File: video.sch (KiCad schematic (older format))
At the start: 42 parts, among them P1 VIDEO OUT, P11 I²C PORT, P2 RGBHV TEST POINTS, U1 VGA SYNC/JOY BUFFER, U2 VGA RGB BUFFER, U3 E-DDC I²C BUFFER

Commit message: Cambios menores
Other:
- note added: "Decoupling capacitors. \nPlace as close as possible to the affected IC pin."
- note added: "U1 (2 of 8)"
- note added: "U2"
- moved on the sheet: C1, C12, C13, C2, C3, C4, C5, C6, C7, R21, R22

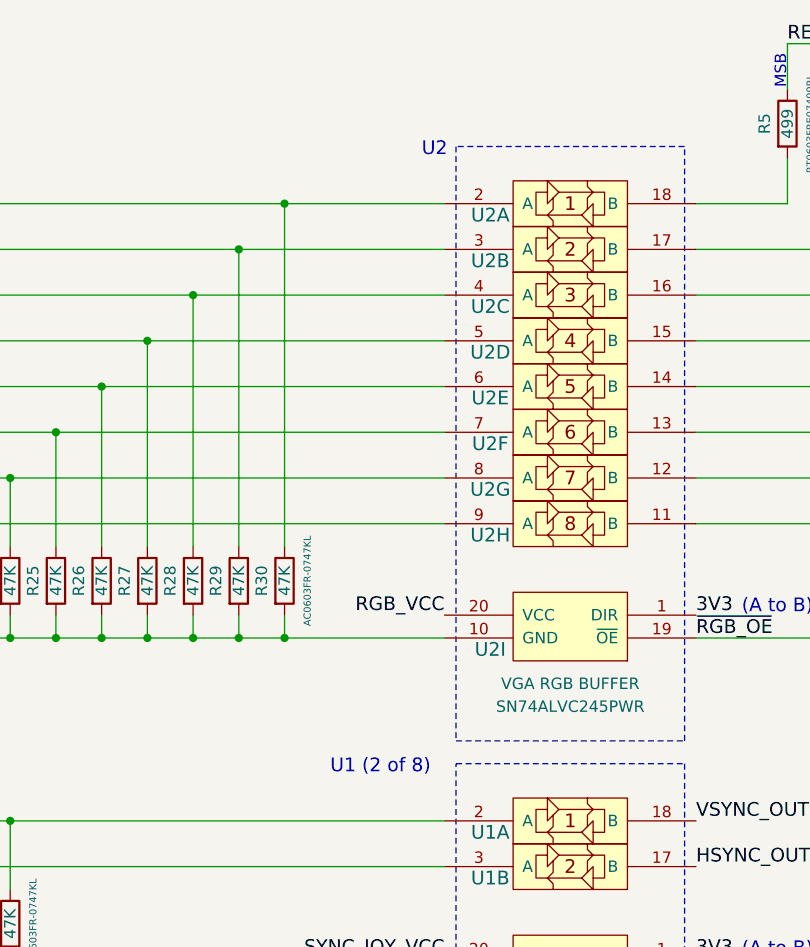
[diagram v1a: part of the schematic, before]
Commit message: Nuevo layout, mejoras y modificaciones del revisor
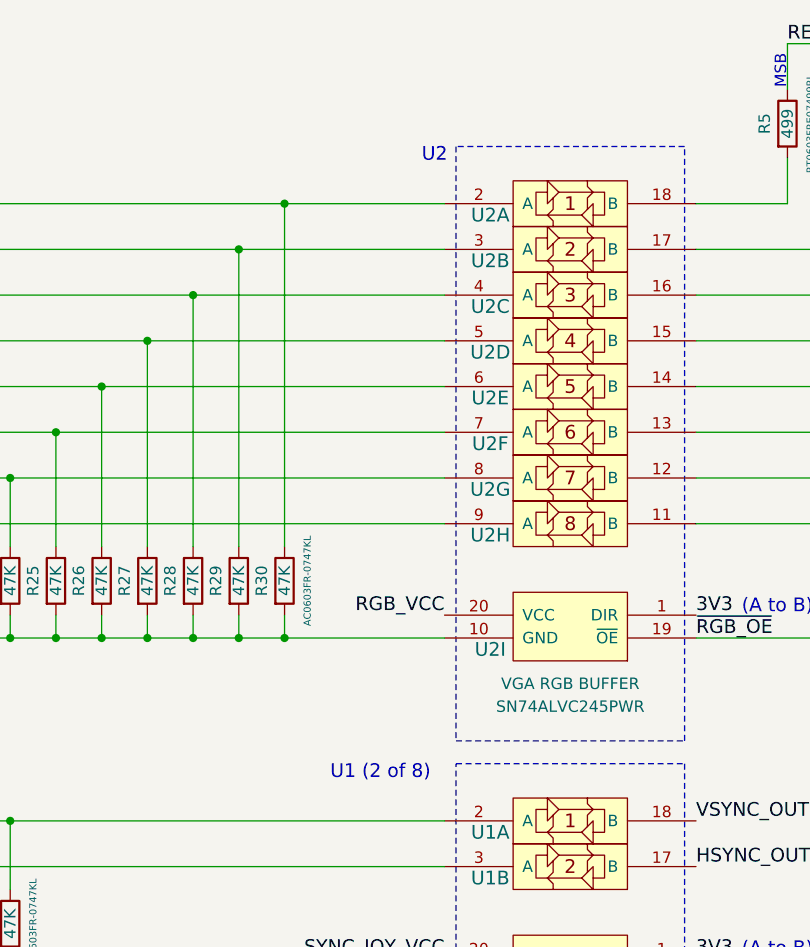
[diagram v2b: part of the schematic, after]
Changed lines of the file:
@@
 LIBS:contrib
 LIBS:valves
-LIBS:salmon
+LIBS:retro-ciaa
 LIBS:retro-ciaa-cache
 EELAYER 25 0
@@
 encoding utf-8
 Sheet 2 8
-Title "RETRO-CIAA / VIDEO"
-Date "2018-10-19"
+Title "VIDEO OUTPUT"
+Date "2018-10-20"
 Rev "1.1.1"
-Comp "Salmon Robotics"
+Comp "http://www.retro-ciaa.com"
 Comment1 "All resistors 1% & 0603\" unless otherwise noted"
 Comment2 "ERC check OK on 2018-10-19"
@@
 Text Notes 1000 7600 0    60   ~ 0
 Decoupling capacitors. \nPlace as close as possible to the affected IC pin.
-Text Notes 3400 1300 0    60   ~ 0
+Text Notes 3400 1325 0    60   ~ 0
 U2
-Text Notes 3000 4000 0    60   ~ 0
+Text Notes 3000 4025 0    60   ~ 0
 U1 (2 of 8)
 $EndSCHEMATC

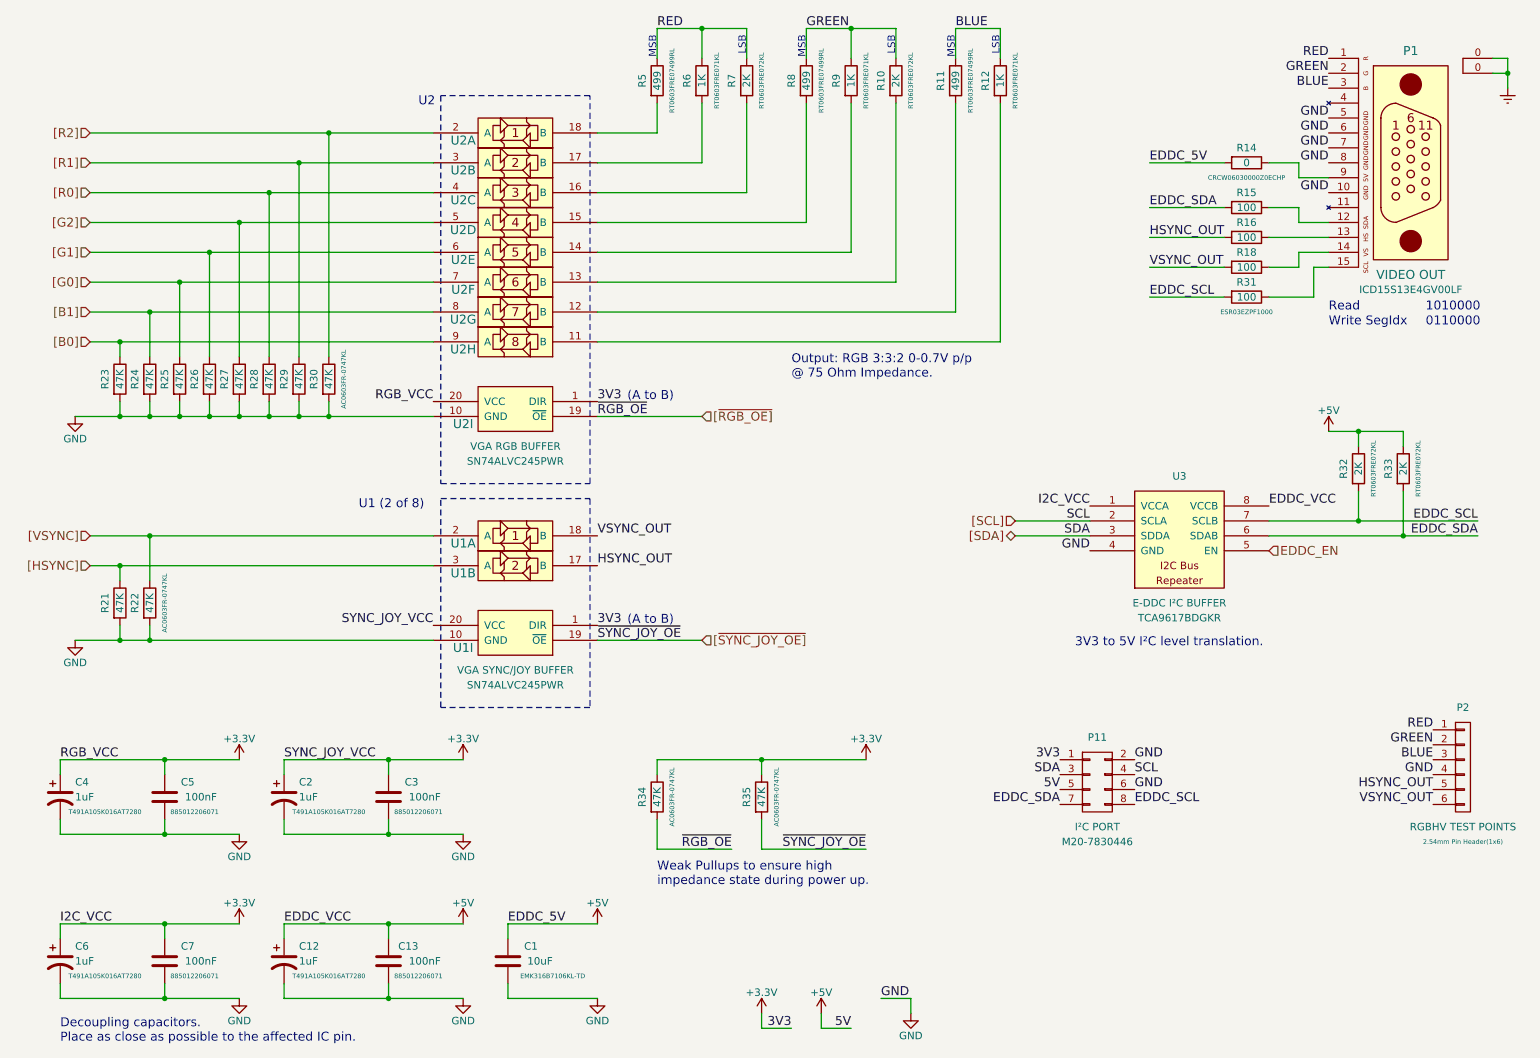
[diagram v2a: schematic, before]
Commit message: Modificacion para clarificar uso de multiparte en U1 y U2
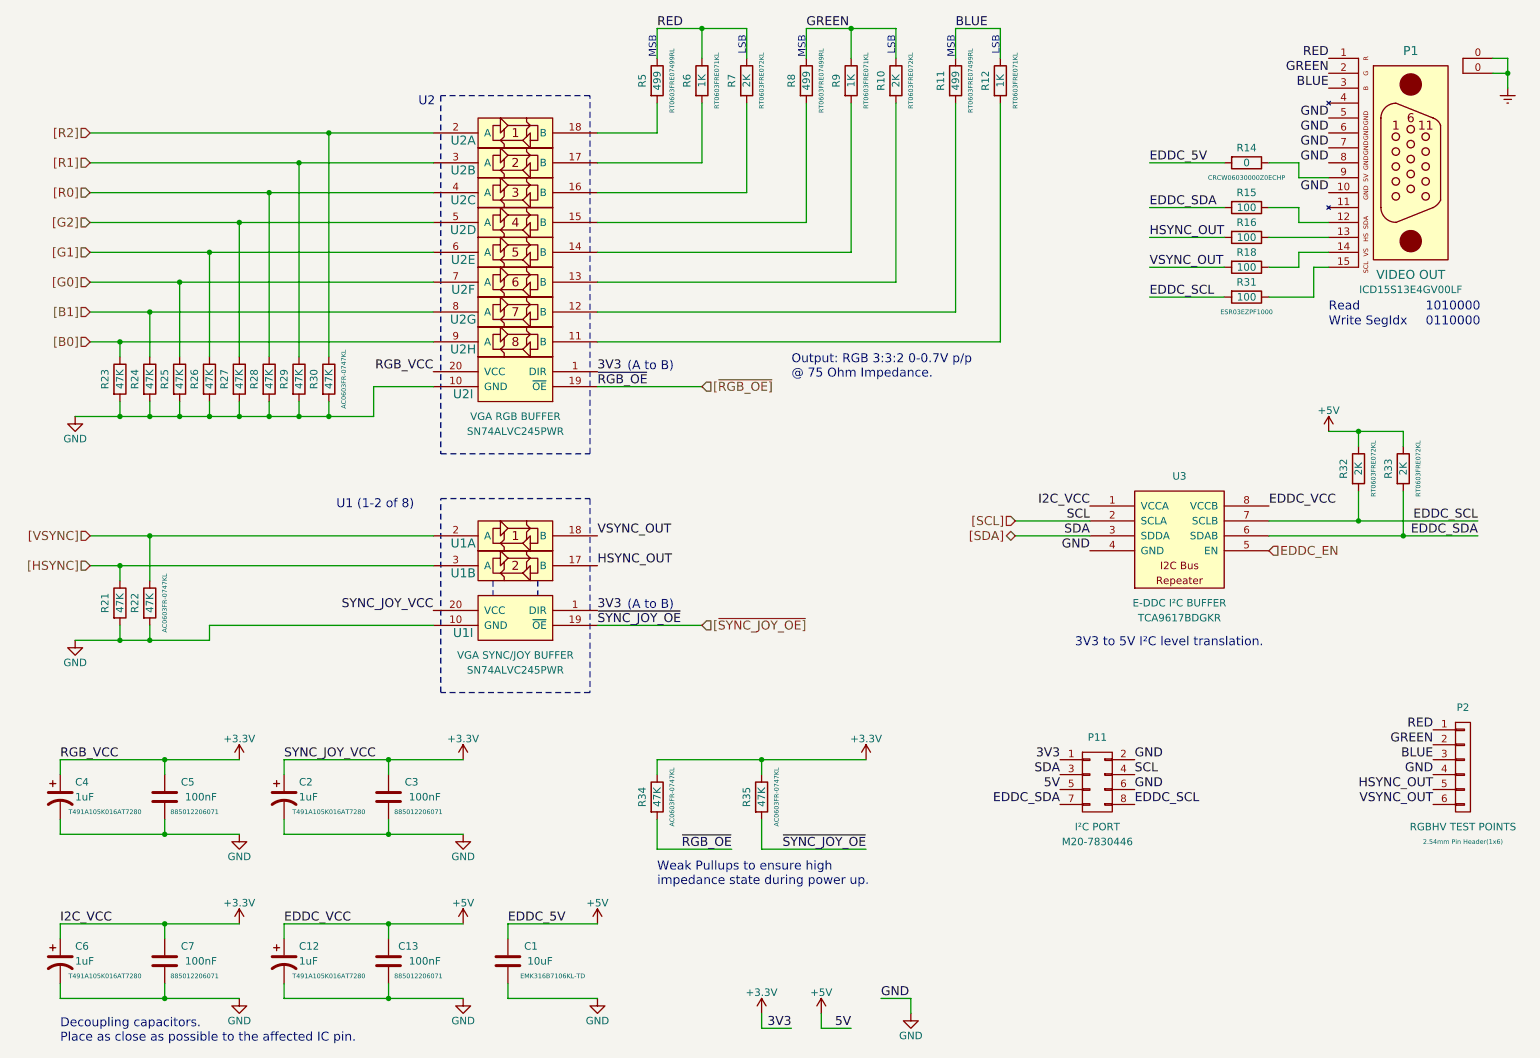
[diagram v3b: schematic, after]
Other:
- note added: "U1 (1-2 of 8)"
- note removed: "U1 (2 of 8)"
- moved on the sheet: U1I, U2I
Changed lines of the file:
@@
 EESchema Schematic File Version 2
-LIBS:retro-ciaa-rescue
 LIBS:power
 LIBS:device
@@
 Text Label 7000 800  0    60   ~ 0
 BLUE
-Text Label 4600 3300 0    60   ~ 0
+Text Label 4600 3100 0    60   ~ 0
 3V3
-Text Label 4600 3400 0    60   ~ 0
+Text Label 4600 3200 0    60   ~ 0
 ~RGB_OE
-Text Label 3500 3300 2    60   ~ 0
+Text Label 3500 3100 2    60   ~ 0
 RGB_VCC
 $Comp
@@
 Text Notes 5900 3150 0    60   ~ 0
 Output: RGB 3:3:2 0-0.7V p/p\n@ 75 Ohm Impedance.
-Text Notes 4800 3300 0    60   ~ 0
+Text Notes 4800 3100 0    60   ~ 0
 (A to B)
 $Comp
@@
 Connection ~ 2800 1500
 Wire Wire Line
-	1100 3400 3500 3400
+	1100 3400 3100 3400
 Wire Wire Line
 	2800 3300 2800 3400
@@
 L SN74ALVC245_MP U2
 U 9 1 5BCF1526
-P 4050 3350
-F 0 "U2" H 3700 3250 60  0000 C CNN
-F 1 "VGA RGB BUFFER" H 4050 3100 50  0000 C CNN
-F 2 "" H 4050 3400 60  0001 C CNN
-F 3 "SN74ALVC245PWR" H 4050 3000 50  0000 C CNN
-	9    4050 3350
+P 4050 3150
+F 0 "U2" H 3700 3050 60  0000 C CNN
+F 1 "VGA RGB BUFFER" H 4050 2900 50  0000 C CNN
+F 2 "" H 4050 3200 60  0001 C CNN
+F 3 "SN74ALVC245PWR" H 4050 2800 50  0000 C CNN
+	9    4050 3150
 	1    0    0    -1
 $EndComp
@@
 	1    0    0    -1
 $EndComp
-Text Label 4600 4800 0    60   ~ 0
+Text Label 4600 4700 0    60   ~ 0
 3V3
-Text Label 3500 4800 2    60   ~ 0
+Text Label 3500 4700 2    60   ~ 0
 SYNC_JOY_VCC
-Text Notes 4800 4800 0    60   ~ 0
+Text Notes 4800 4700 0    60   ~ 0
 (A to B)
 Text Label 4600 4400 0    60   ~ 0
@@
 Text Label 4600 4200 0    60   ~ 0
 VSYNC_OUT
-Text Label 4600 4900 0    60   ~ 0
+Text Label 4600 4800 0    60   ~ 0
 ~SYNC_JOY_OE
 Wire Wire Line
@@
 L SN74ALVC245_MP U1
 U 9 1 5BCFFF19
-P 4050 4850
+P 4050 4750
 AR Path="/5BCCB2EC/5BCFFF19" Ref="U1"  Part="9"
 AR Path="/5BCFFF19" Ref="U?"  Part="9"
-F 0 "U1" H 3700 4750 60  0000 C CNN
-F 1 "VGA SYNC/JOY BUFFER" H 4050 4600 50  0000 C CNN
-F 2 "" H 4050 4900 60  0001 C CNN
-F 3 "SN74ALVC245PWR" H 4050 4500 50  0000 C CNN
-	9    4050 4850
+F 0 "U1" H 3700 4650 60  0000 C CNN
+F 1 "VGA SYNC/JOY BUFFER" H 4050 4500 50  0000 C CNN
+F 2 "" H 4050 4800 60  0001 C CNN
+F 3 "SN74ALVC245PWR" H 4050 4400 50  0000 C CNN
+	9    4050 4750
 	1    0    0    -1
 $EndComp
@@
 $EndComp
 Wire Wire Line
-	1100 4900 3500 4900
+	1100 4900 2000 4900
 Connection ~ 1400 4900
 Connection ~ 1600 4900
@@
 Text HLabel 9100 4300 2    60   Input ~ 0
 EDDC_EN
-Text HLabel 5300 3400 2    60   Input ~ 0
+Text HLabel 5300 3200 2    60   Input ~ 0
 [~RGB_OE]
-Text HLabel 5300 4900 2    60   Input ~ 0
+Text HLabel 5300 4800 2    60   Input ~ 0
 [~SYNC_JOY_OE]
 Wire Wire Line
-	5300 3400 4600 3400
-Wire Wire Line
-	5300 4900 4600 4900
+	5300 3200 4600 3200
+Wire Wire Line
+	5300 4800 4600 4800
 Wire Wire Line
 	7400 4100 7900 4100
@@
 	6700 7300 6700 7400
 Wire Notes Line
-	3550 1250 3550 3850
+	3550 1250 3550 3650
 Wire Notes Line
-	3550 3850 4550 3850
+	3550 3650 4550 3650
 Wire Notes Line
-	4550 3850 4550 1250
+	4550 3650 4550 1250
 Wire Notes Line
 	4550 1250 3550 1250
@@
 	3550 3950 4550 3950
 Wire Notes Line
-	4550 3950 4550 5350
+	4550 3950 4550 5250
 Wire Notes Line
-	4550 5350 3550 5350
+	4550 5250 3550 5250
 Wire Notes Line
-	3550 5350 3550 3950
+	3550 5250 3550 3950
 Text Notes 1000 7600 0    60   ~ 0
 Decoupling capacitors. \nPlace as close as possible to the affected IC pin.
 Text Notes 3400 1325 0    60   ~ 0
 U2
-Text Notes 3000 4025 0    60   ~ 0
-U1 (2 of 8)
+Text Notes 2850 4025 0    60   ~ 0
+U1 (1-2 of 8)
+Wire Wire Line
+	3100 3400 3100 3200
+Wire Wire Line
+	3100 3200 3500 3200
+Wire Wire Line
+	2000 4900 2000 4800
+Wire Wire Line
+	2000 4800 3500 4800
+Wire Notes Line
+	3900 4500 3900 4600
+Wire Notes Line
+	4200 4500 4200 4600
 $EndSCHEMATC
